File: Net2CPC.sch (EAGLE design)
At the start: 22 parts, among them CON1 CPCBUS, IC1 74HCT30N, IC2 74LS32N, IC3 74LS32N, IC4 AMS1117-3.3

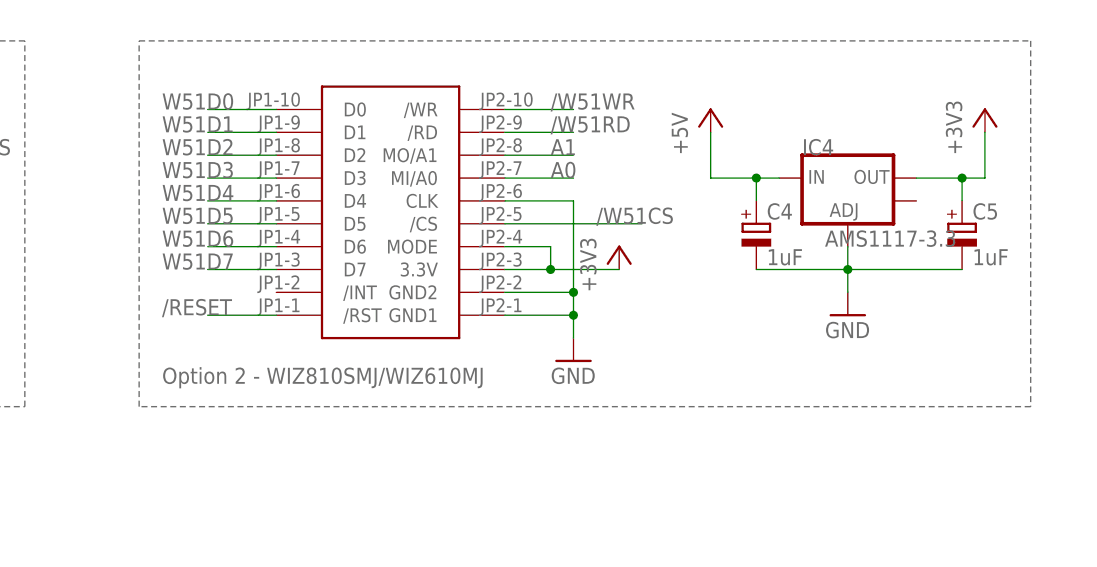
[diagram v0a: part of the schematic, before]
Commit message: Add files via upload
Added voltage value to electrolytic caps.
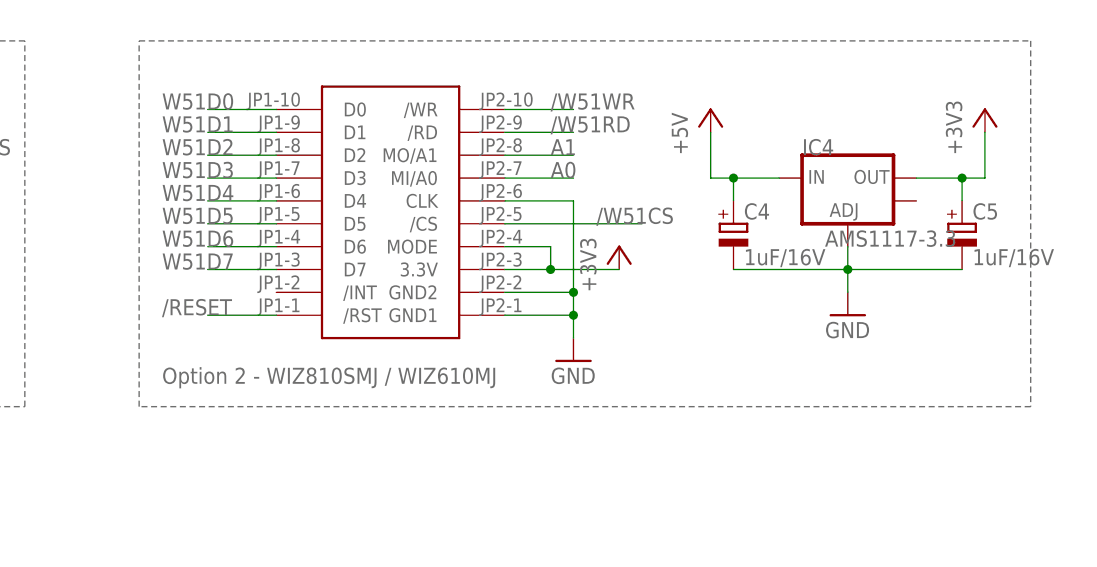
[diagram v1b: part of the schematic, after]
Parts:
- C4, C5: value 1uF -> 1uF/16V
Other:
- note added: "Option 2 - WIZ810SMJ / WIZ610MJ"
- note removed: "Option 2 - WIZ810SMJ/WIZ610MJ"
- moved on the sheet: C4
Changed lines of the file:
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@@
 <part name="P+4" library="supply1" library_urn="urn:adsk.eagle:library:371" deviceset="+5V" device=""/>
 <part name="IC4" library="SparkFun" deviceset="V_REG_LM1117" device="SOT223" value="AMS1117-3.3"/>
-<part name="C4" library="rcl" library_urn="urn:adsk.eagle:library:334" deviceset="CPOL-EU" device="E5-6" package3d_urn="urn:adsk.eagle:package:23368/1" value="1uF"/>
-<part name="C5" library="rcl" library_urn="urn:adsk.eagle:library:334" deviceset="CPOL-EU" device="E5-6" package3d_urn="urn:adsk.eagle:package:23368/1" value="1uF"/>
+<part name="C4" library="rcl" library_urn="urn:adsk.eagle:library:334" deviceset="CPOL-EU" device="E5-6" package3d_urn="urn:adsk.eagle:package:23368/1" value="1uF/16V"/>
+<part name="C5" library="rcl" library_urn="urn:adsk.eagle:library:334" deviceset="CPOL-EU" device="E5-6" package3d_urn="urn:adsk.eagle:package:23368/1" value="1uF/16V"/>
 </parts>
 <sheets>
@@
 <wire x1="142.24" y1="66.04" x2="142.24" y2="106.68" width="0.1524" layer="95" style="shortdash"/>
 <text x="83.82" y="68.58" size="1.778" layer="95">Option 1 -W5100S Ethernet Module</text>
-<text x="157.48" y="68.58" size="1.778" layer="95">Option 2 - WIZ810SMJ/WIZ610MJ</text>
+<text x="157.48" y="68.58" size="1.778" layer="95">Option 2 - WIZ810SMJ / WIZ610MJ</text>
 </plain>
 <instances>
@@
 <attribute name="VALUE" x="231.14" y="83.82" size="1.778" layer="96"/>
 </instance>
-<instance part="C4" gate="G$1" x="223.52" y="86.36" smashed="yes">
-<attribute name="NAME" x="224.663" y="86.8426" size="1.778" layer="95"/>
-<attribute name="VALUE" x="224.663" y="81.7626" size="1.778" layer="96"/>
+<instance part="C4" gate="G$1" x="220.98" y="86.36" smashed="yes">
+<attribute name="NAME" x="222.123" y="86.8426" size="1.778" layer="95"/>
+<attribute name="VALUE" x="222.123" y="81.7626" size="1.778" layer="96"/>
 </instance>
 <instance part="C5" gate="G$1" x="246.38" y="86.36" smashed="yes">
@@
 <pinref part="C4" gate="G$1" pin="-"/>
 <wire x1="233.68" y1="81.28" x2="233.68" y2="78.74" width="0.1524" layer="91"/>
-<wire x1="223.52" y1="81.28" x2="233.68" y2="81.28" width="0.1524" layer="91"/>
+<wire x1="220.98" y1="81.28" x2="233.68" y2="81.28" width="0.1524" layer="91"/>
 <junction x="233.68" y="81.28"/>
 <pinref part="C5" gate="G$1" pin="-"/>
@@
 <pinref part="P+4" gate="1" pin="+5V"/>
 <pinref part="IC4" gate="G$1" pin="IN"/>
-<wire x1="226.06" y1="91.44" x2="223.52" y2="91.44" width="0.1524" layer="91"/>
+<wire x1="226.06" y1="91.44" x2="220.98" y2="91.44" width="0.1524" layer="91"/>
 <pinref part="C4" gate="G$1" pin="+"/>
-<wire x1="223.52" y1="91.44" x2="218.44" y2="91.44" width="0.1524" layer="91"/>
-<wire x1="223.52" y1="88.9" x2="223.52" y2="91.44" width="0.1524" layer="91"/>
-<junction x="223.52" y="91.44"/>
-</segment>
-</net>
+<wire x1="220.98" y1="91.44" x2="218.44" y2="91.44" width="0.1524" layer="91"/>
+<wire x1="220.98" y1="88.9" x2="220.98" y2="91.44" width="0.1524" layer="91"/>
+<junction x="220.98" y="91.44"/>
+</segment>
+</net>

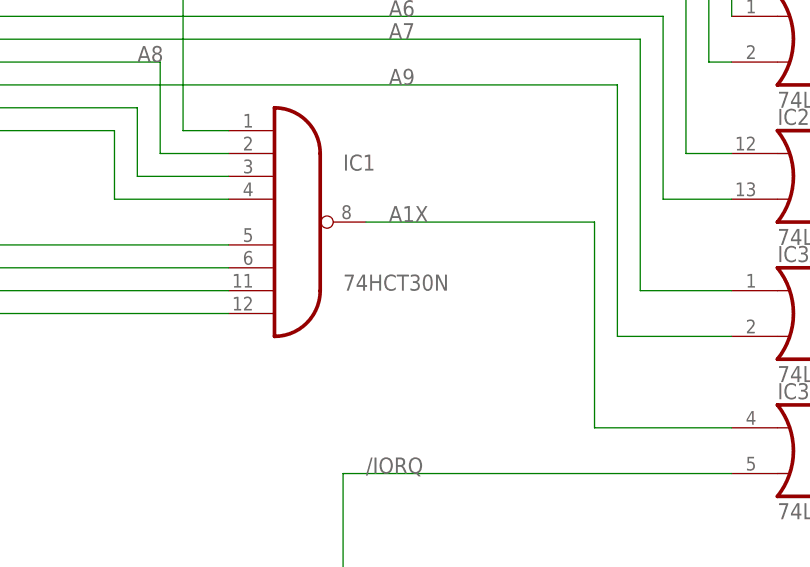
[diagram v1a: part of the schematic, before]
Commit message: Add files via upload
Changed IC1 type
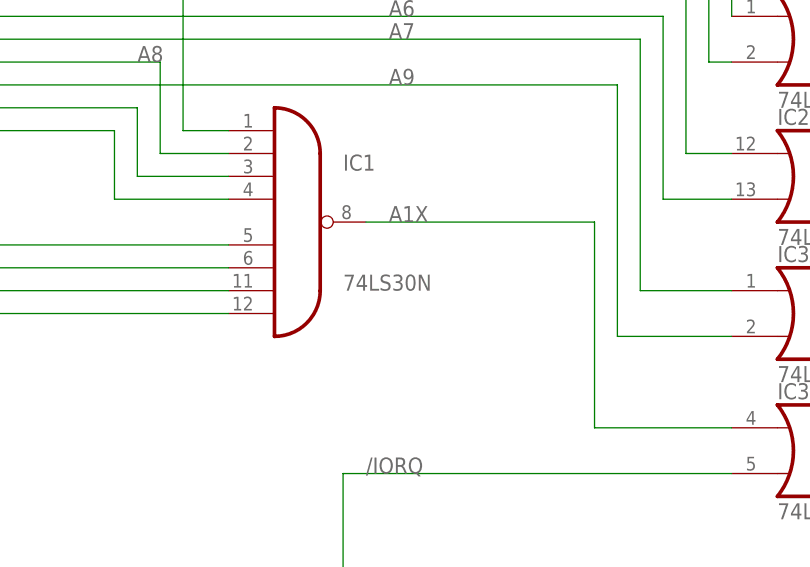
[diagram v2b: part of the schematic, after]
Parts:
- IC1: value 74HCT30N -> 74LS30N
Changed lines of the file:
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@@
 <grid distance="0.1" unitdist="inch" unit="inch" style="lines" multiple="1" display="no" altdistance="0.01" altunitdist="inch" altunit="inch"/>
 <layers>
-<layer number="1" name="Top" color="4" fill="1" visible="yes" active="no"/>
-<layer number="16" name="Bottom" color="1" fill="1" visible="yes" active="no"/>
-<layer number="17" name="Pads" color="2" fill="1" visible="yes" active="no"/>
-<layer number="18" name="Vias" color="2" fill="1" visible="yes" active="no"/>
-<layer number="19" name="Unrouted" color="6" fill="1" visible="yes" active="no"/>
-<layer number="20" name="Dimension" color="15" fill="1" visible="yes" active="no"/>
-<layer number="21" name="tPlace" color="7" fill="1" visible="yes" active="no"/>
-<layer number="22" name="bPlace" color="7" fill="1" visible="yes" active="no"/>
-<layer number="23" name="tOrigins" color="15" fill="1" visible="yes" active="no"/>
-<layer number="24" name="bOrigins" color="15" fill="1" visible="yes" active="no"/>
-<layer number="25" name="tNames" color="7" fill="1" visible="yes" active="no"/>
-<layer number="26" name="bNames" color="7" fill="1" visible="yes" active="no"/>
-<layer number="27" name="tValues" color="7" fill="1" visible="yes" active="no"/>
-<layer number="28" name="bValues" color="7" fill="1" visible="yes" active="no"/>
+<layer number="1" name="Top" color="4" fill="1" visible="no" active="no"/>
+<layer number="16" name="Bottom" color="1" fill="1" visible="no" active="no"/>
+<layer number="17" name="Pads" color="2" fill="1" visible="no" active="no"/>
+<layer number="18" name="Vias" color="2" fill="1" visible="no" active="no"/>
+<layer number="19" name="Unrouted" color="6" fill="1" visible="no" active="no"/>
+<layer number="20" name="Dimension" color="15" fill="1" visible="no" active="no"/>
+<layer number="21" name="tPlace" color="7" fill="1" visible="no" active="no"/>
+<layer number="22" name="bPlace" color="7" fill="1" visible="no" active="no"/>
+<layer number="23" name="tOrigins" color="15" fill="1" visible="no" active="no"/>
+<layer number="24" name="bOrigins" color="15" fill="1" visible="no" active="no"/>
+<layer number="25" name="tNames" color="7" fill="1" visible="no" active="no"/>
+<layer number="26" name="bNames" color="7" fill="1" visible="no" active="no"/>
+<layer number="27" name="tValues" color="7" fill="1" visible="no" active="no"/>
+<layer number="28" name="bValues" color="7" fill="1" visible="no" active="no"/>
 <layer number="29" name="tStop" color="7" fill="3" visible="no" active="no"/>
 <layer number="30" name="bStop" color="7" fill="6" visible="no" active="no"/>
@@
 <layer number="35" name="tGlue" color="7" fill="4" visible="no" active="no"/>
 <layer number="36" name="bGlue" color="7" fill="5" visible="no" active="no"/>
-<layer number="37" name="tTest" color="7" fill="1" visible="yes" active="no"/>
-<layer number="38" name="bTest" color="7" fill="1" visible="yes" active="no"/>
+<layer number="37" name="tTest" color="7" fill="1" visible="no" active="no"/>
+<layer number="38" name="bTest" color="7" fill="1" visible="no" active="no"/>
 <layer number="39" name="tKeepout" color="4" fill="11" visible="no" active="no"/>
 <layer number="40" name="bKeepout" color="1" fill="11" visible="no" active="no"/>
@@
 <layer number="44" name="Drills" color="7" fill="1" visible="no" active="no"/>
 <layer number="45" name="Holes" color="7" fill="1" visible="no" active="no"/>
-<layer number="46" name="Milling" color="3" fill="1" visible="yes" active="no"/>
-<layer number="47" name="Measures" color="7" fill="1" visible="yes" active="no"/>
-<layer number="48" name="Document" color="7" fill="1" visible="yes" active="no"/>
-<layer number="49" name="Reference" color="7" fill="1" visible="yes" active="no"/>
-<layer number="50" name="dxf" color="7" fill="1" visible="yes" active="no"/>
-<layer number="51" name="tDocu" color="7" fill="1" visible="yes" active="no"/>
-<layer number="52" name="bDocu" color="7" fill="1" visible="yes" active="no"/>
-<layer number="53" name="tGND_GNDA" color="7" fill="9" visible="yes" active="no"/>
-<layer number="54" name="bGND_GNDA" color="1" fill="9" visible="yes" active="no"/>
-<layer number="56" name="wert" color="7" fill="1" visible="yes" active="no"/>
+<layer number="46" name="Milling" color="3" fill="1" visible="no" active="no"/>
+<layer number="47" name="Measures" color="7" fill="1" visible="no" active="no"/>
+<layer number="48" name="Document" color="7" fill="1" visible="no" active="no"/>
+<layer number="49" name="Reference" color="7" fill="1" visible="no" active="no"/>
+<layer number="50" name="dxf" color="7" fill="1" visible="no" active="no"/>
+<layer number="51" name="tDocu" color="7" fill="1" visible="no" active="no"/>
+<layer number="52" name="bDocu" color="7" fill="1" visible="no" active="no"/>
+<layer number="53" name="tGND_GNDA" color="7" fill="9" visible="no" active="no"/>
+<layer number="54" name="bGND_GNDA" color="1" fill="9" visible="no" active="no"/>
+<layer number="56" name="wert" color="7" fill="1" visible="no" active="no"/>
 <layer number="88" name="SimResults" color="9" fill="1" visible="yes" active="yes"/>
 <layer number="89" name="SimProbes" color="9" fill="1" visible="yes" active="yes"/>
@@
 <attribute name="TITLE" value="Net4CPC"/>
 </part>
-<part name="IC1" library="74xx-eu" library_urn="urn:adsk.eagle:library:85" deviceset="74*30" device="N" package3d_urn="urn:adsk.eagle:package:16407/2" technology="HCT"/>
+<part name="IC1" library="74xx-eu" library_urn="urn:adsk.eagle:library:85" deviceset="74*30" device="N" package3d_urn="urn:adsk.eagle:package:16407/2" technology="HCT" value="74LS30N"/>
 <part name="IC2" library="74xx-us" library_urn="urn:adsk.eagle:library:88" deviceset="74*32" device="N" package3d_urn="urn:adsk.eagle:package:16407/2" technology="LS"/>
 <part name="IC3" library="74xx-us" library_urn="urn:adsk.eagle:library:88" deviceset="74*32" device="N" package3d_urn="urn:adsk.eagle:package:16407/2" technology="LS"/>
